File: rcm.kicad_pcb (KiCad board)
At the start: 2 copper layers, 140 x 70 mm, 158 parts, among them Y1 8MHz, Y2 32.768kHz

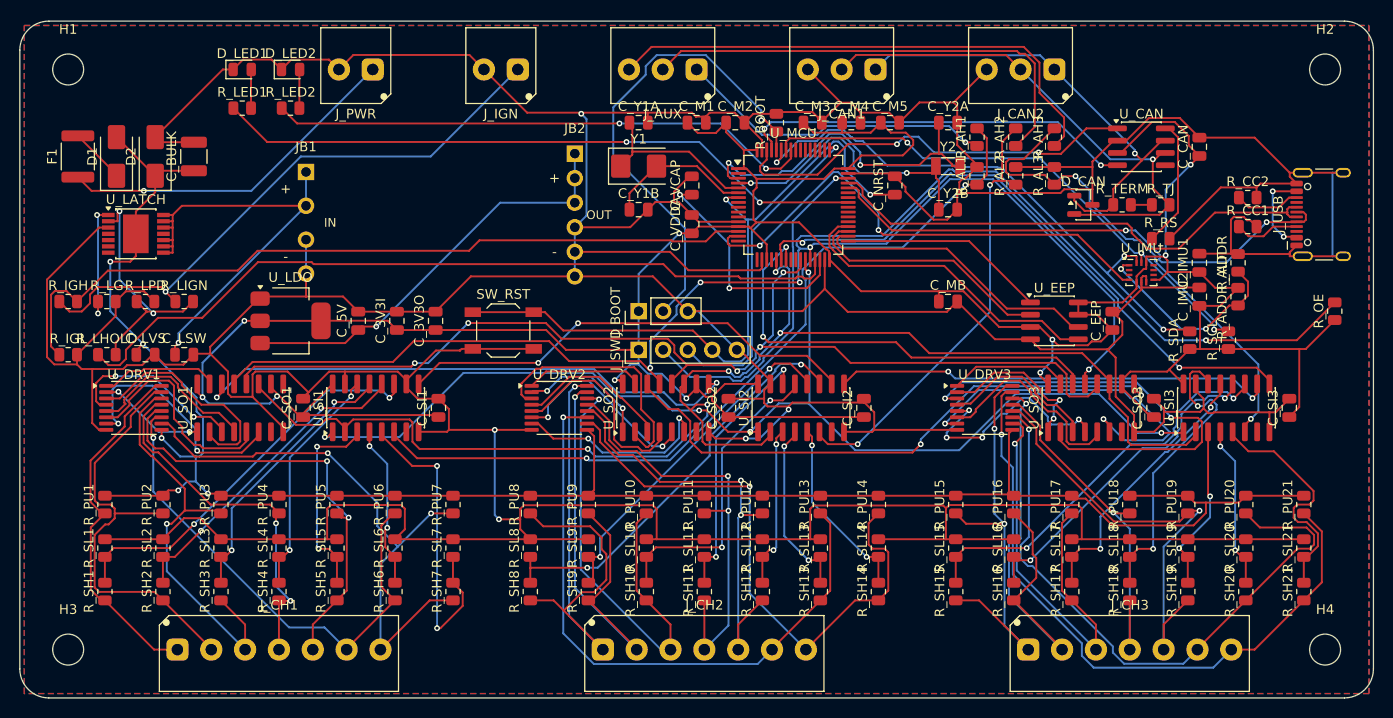
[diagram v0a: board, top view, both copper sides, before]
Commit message: rcm: shift the MCU into the dead space, and fix the button pull-up for wetting current
MCU moved right and down into the empty area, away from the tight strip above it.
The decoupling row and R_BOOT are now positioned relative to the MCU so the BOOT0
escape lane fixed last round travels with it. Round 6 routes 414/414 with 0
unconnected and 0 DRC errors, in 2149 segments - fewer than before, so the move
improved routability slightly.

Button pull-up 100k -> 10k. At 12V a 100k pull-up passes only ~120uA through a
closed contact, below the ~1mA most mechanical contacts need to break through
surface film. Gold contacts are fine at microamps, ordinary automotive buttons
are not, and it fails in the worst way: perfect on the bench, intermittent months
later in a damp vibrating car. 10k gives 1.2mA on press and does not move the
logic levels. Patched into the placed board in-place rather than regenerating,
which would have wiped the routing.

Recorded the answer on momentary buttons: they work, and they beat a mechanical
latching switch because a latched switch can be physically stuck in the wrong
position when something else changes the state, whereas a momentary button has
no position to be wrong about. Also noted debouncing is mandatory and that each
button costs two channels.

Co-Authored-By: Claude Opus 5 <noreply@anthropic.com>
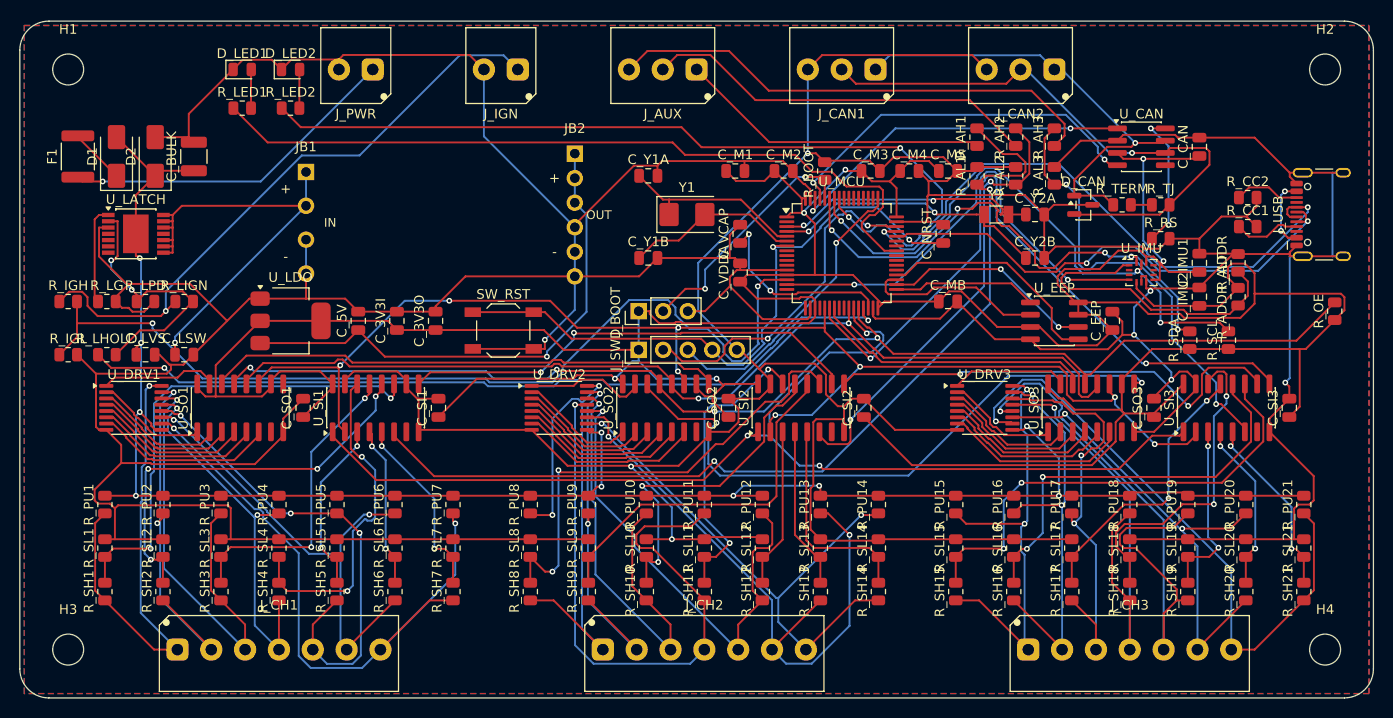
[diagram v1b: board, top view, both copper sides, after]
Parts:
- R_PU1, R_PU10, R_PU11, R_PU12, R_PU13, R_PU14, R_PU15, R_PU16, R_PU17, R_PU18, R_PU19, R_PU2, R_PU20, R_PU21, R_PU3, R_PU4, R_PU5, R_PU6, R_PU7, R_PU8, R_PU9: value 100k -> 10k
- moved C_Y2A 13.1 mm to (105.0, 20.0)
- moved C_Y2B 10.3 mm to (105.0, 24.5)
- moved C_M3 7.81 mm to (88.0, 15.5)
- moved C_M4 7.81 mm to (92.0, 15.5)
- moved C_M5 7.81 mm to (96.0, 15.5)
- moved C_M2 7.07 mm to (79.0, 15.5)
- moved C_NRST 7.07 mm to (95.5, 22.0)
- moved C_VCAP 7.07 mm to (74.5, 22.0)
- moved C_VDDA 7.07 mm to (74.5, 26.0)
- moved R_BOOT 7.07 mm to (83.2, 15.5)
- moved U_MCU 7.07 mm to (85.0, 24.0)
- moved Y1 7.07 mm to (69.0, 20.0)
- moved Y2 7.07 mm to (101.0, 20.0)
- moved C_M1 6.40 mm to (74.0, 15.5)
- moved C_Y1A 5.59 mm to (65.0, 16.0)
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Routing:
- net +3V3: track 352.5 -> 425.4 mm, vias 10 -> 6
- net SR_OE_N: track 193.8 -> 130.7 mm, vias 6 -> 4
- net DRV17: track 48.6 -> 13.7 mm, vias 2 -> 0
- net LED2: track 56.6 -> 89.4 mm
- net BOOT0: track 50.5 -> 25.7 mm, vias 1 -> 2
- net CH11: track 45.5 -> 64.4 mm, vias 2 -> 1
- net DRV21: track 37.5 -> 19.3 mm, vias 2 -> 0
- net SR_MOSI: track 46.2 -> 29.1 mm, vias 2 -> 0
- net CH19: track 47.5 -> 64.5 mm
- net IGN_SENSE: track 81.4 -> 97.0 mm, vias 0 -> 2
- net CH20: track 65.4 -> 50.2 mm, vias 1 -> 2
- net ASNS1: track 84.0 -> 98.5 mm
- net SNS7: track 33.3 -> 19.3 mm
- net LED1: track 67.6 -> 80.4 mm, vias 2 -> 0
- net DRV10: track 26.3 -> 13.6 mm
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
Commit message: rcm: MCU-east cluster spread out, and fix the THT thermal bug properly
Rehomed the six aux-input dividers from x~99-107 - where they sat on top of the
MCU - into a single row under J_AUX at x=70, which is the connector they actually
belong to. That was a routing inefficiency as much as a crowding one. The CAN and
IMU groups then spread west into the space it freed.

Round 9: 414/414 nets, 0 unconnected, 0 DRC errors, 2231 segments.

Fixed fix_starved_thermals.py rather than the board. The DRC report writes
"PTH pad 5 [GND] of J_SWD" for through-hole but "Pad 12 [GND] of U1" for SMD, and
the parser only matched the latter - so it reported "nothing to do" while every
THT violation remained. I had patched the board by hand last time; regenerating
wiped it, which is the lesson: manual board edits do not survive, the fix belongs
in the pipeline. Patched here and in the shared toolkit.

Also worth recording against my own process: I nudged C_Y2B seven times by
guesswork, once landing it on top of the MCU, which cost a 2m40s routing run that
came back with two broken nets. Computing a free position takes seconds and
should have been the first move, not the eighth.

Co-Authored-By: Claude Opus 5 <noreply@anthropic.com>
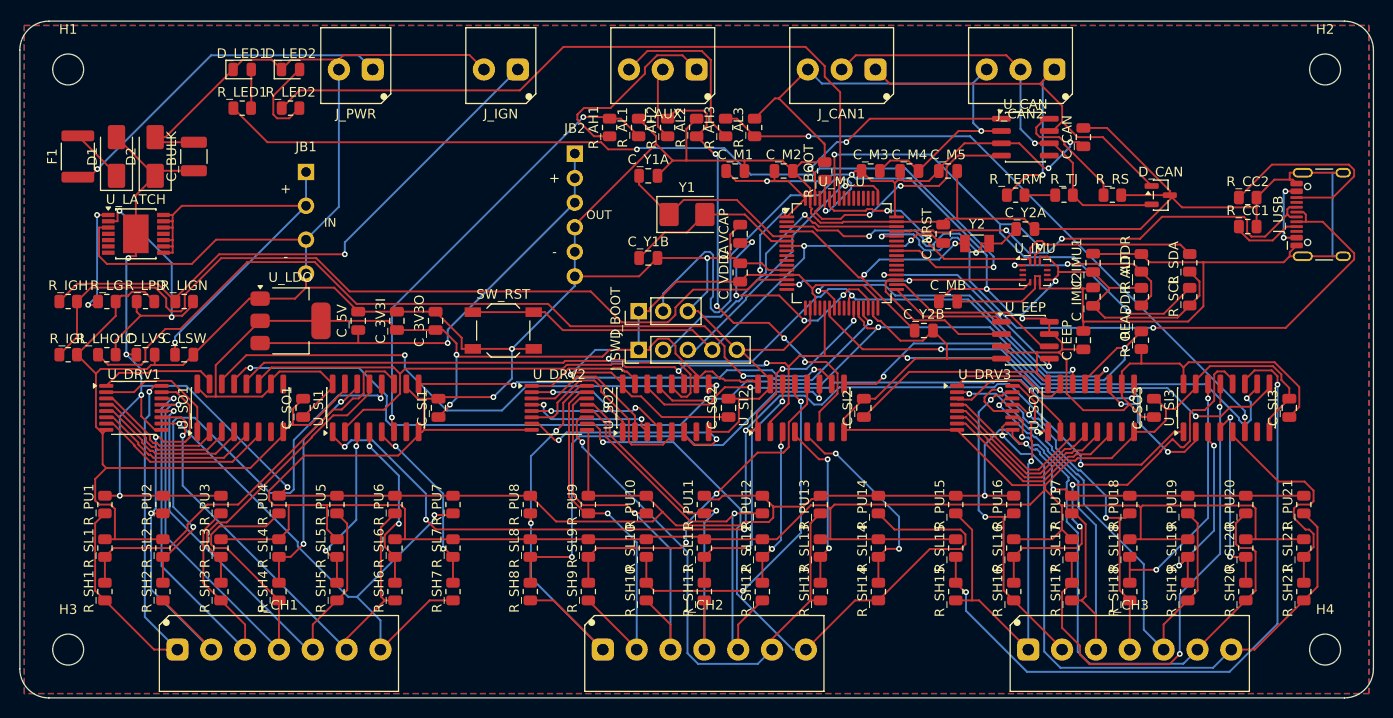
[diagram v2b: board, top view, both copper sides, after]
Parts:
- moved R_AH1 38.0 mm to (61.0, 11.0)
- moved R_AH2 36.0 mm to (67.0, 11.0)
- moved R_AL1 35.4 mm to (64.0, 11.0)
- moved R_AH3 34.0 mm to (73.0, 11.0)
- moved R_AL2 33.4 mm to (70.0, 11.0)
- moved R_AL3 31.4 mm to (76.0, 11.0)
- moved R_OE 20.2 mm to (116.0, 33.0)
- moved C_Y2B 13.7 mm to (93.5, 32.0)
- moved C_CAN 12.0 mm to (110.0, 12.0)
- moved U_CAN 12.0 mm to (104.0, 12.0)
- moved R_TERM 11.0 mm to (103.0, 18.0)
- moved C_IMU1 11.0 mm to (111.0, 25.0)
- moved C_IMU2 11.0 mm to (111.0, 28.5)
- moved U_IMU 11.0 mm to (105.0, 26.0)
- moved R_TJ 10.0 mm to (108.0, 18.0)
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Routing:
- net ASNS1: track 98.5 -> 47.4 mm
- net +3V3: track 425.4 -> 381.3 mm, vias 6 -> 12
- net +12V_P: track 196.8 -> 233.6 mm, vias 10 -> 8
- net GND: track 849.7 -> 886.1 mm, vias 8 -> 4
- net AUX3: track 51.7 -> 18.2 mm
- net AUX2: track 41.0 -> 7.54 mm
- net CH11: track 64.4 -> 38.9 mm
- net SNS15: track 49.1 -> 73.0 mm
- net IMU_INT1: track 48.2 -> 24.6 mm
- net SNS17: track 29.3 -> 52.2 mm
- net ASNS3: track 45.6 -> 68.4 mm
- net BOOT0: track 25.7 -> 45.2 mm, vias 2 -> 1
- net SR_MISO: track 71.6 -> 52.3 mm
- net USB_DM: track 51.4 -> 70.4 mm
- net LED1: track 80.4 -> 97.5 mm, vias 0 -> 2
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
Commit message: rcm: put both crystals beside their own pins - placement complete
Read the MCU pin positions off the placed board: PC14/PC15 (LSE) and PH0/PH1
(HSE) are all on the chip's west edge. Y1 was 14mm away and Y2 was on the wrong
side of the chip entirely at 20mm, with its signals crossing the whole package.
Both are now 6.8mm from their pins. Nothing ever flagged this - both were legally
placed and fully routed throughout.

C_VCAP and C_VDDA moved south of the MCU to free that edge. The actual blocker
turned out to be J_BOOT, a 3-pin jumper with no placement constraints at all;
several attempts went into fitting a capacitor around it before moving the jumper
solved it at once.

Also settled the question of when to retry the router, since this board has now
produced one of each: BOOT0 failed three runs with byte-identical output, which
means deterministic and retrying is useless - the cause was a 0.6mm escape slot.
LATCH_GND failed once and routed on the next run with a different score, which
means stochastic. The test is one re-run and a comparison of the numbers, not a
guess.

414/414 nets, 0 unconnected, 0 DRC errors. Placement is done.

Co-Authored-By: Claude Opus 5 <noreply@anthropic.com>
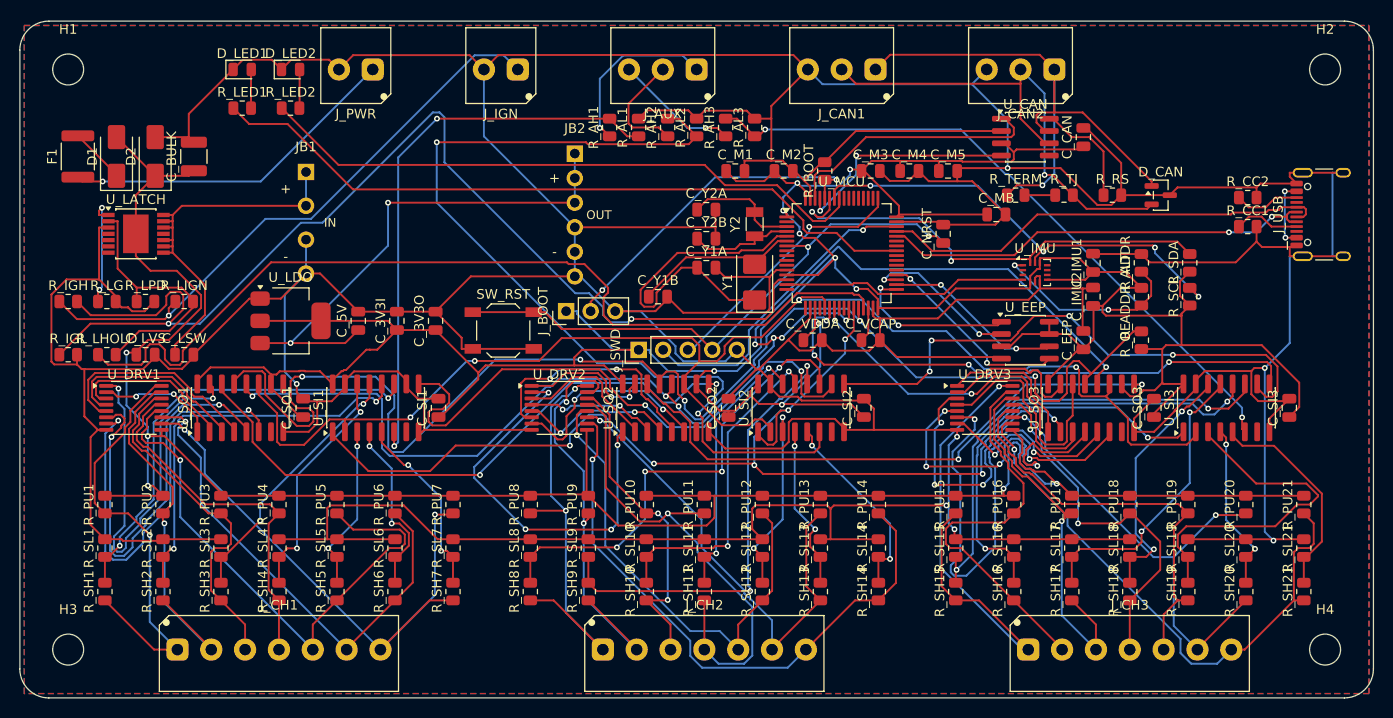
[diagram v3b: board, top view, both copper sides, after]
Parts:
- moved C_Y2A 33.1 mm to (71.0, 19.5)
- moved C_Y2B 24.4 mm to (71.0, 22.5)
- moved Y2 23.1 mm to (76.0, 21.0), turned to 90 degrees
- moved C_VCAP 17.4 mm to (88.0, 33.0), turned to 0 degrees
- moved C_Y1A 11.2 mm to (71.0, 25.5)
- moved C_MB 10.3 mm to (101.0, 20.0)
- moved C_VDDA 10.3 mm to (82.0, 33.0), turned to 0 degrees
- moved Y1 9.90 mm to (76.0, 27.0), turned to 90 degrees
- moved J_BOOT 7.50 mm to (56.5, 30.0)
- moved C_Y1B 4.12 mm to (66.0, 28.5)
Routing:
- net ASNS2: track 48.3 -> 96.4 mm, vias 4 -> 2
- net DRV20: track 19.3 -> 50.9 mm, vias 0 -> 2
- net DRV1: track 12.1 -> 42.8 mm, vias 0 -> 2
- net DRV9: track 11.7 -> 40.8 mm, vias 2 -> 4
- net IGN_SENSE: track 89.9 -> 118.1 mm, vias 0 -> 2
- net DRV6: track 17.7 -> 44.2 mm, vias 0 -> 2
- net DRV7: track 19.0 -> 45.4 mm, vias 0 -> 2
- net USB_DM: track 70.4 -> 45.5 mm
- net SNS15: track 73.0 -> 48.5 mm
- net LED1: track 97.5 -> 75.2 mm, vias 2 -> 0
- net SNS17: track 52.2 -> 30.6 mm
- net VCAP1: track 24.9 -> 3.61 mm, vias 4 -> 0
- net SR_OE_N: track 123.7 -> 142.7 mm, vias 4 -> 5
- net SR_RCLK: track 114.7 -> 133.6 mm, vias 3 -> 8
- net LSE_OUT: track 29.6 -> 10.9 mm, vias 2 -> 0
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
